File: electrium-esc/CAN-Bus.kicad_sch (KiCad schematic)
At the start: 0 parts

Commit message: Add additional connections to MCU
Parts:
- added C? (x3): 100n, symbol Device:C
- added R? (x2): 10, symbol Device:R
- added R?: IN, symbol Device:R
- added U?: SN65HVD232, Package_SO:SOIC-8_3.9x4.9mm_P1.27mm, symbol Interface_CAN_LIN:SN65HVD232
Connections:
- new net: C?.2, R?.2, U?.1 (D)
- new net: R?.1, U?.4 (R)
- new net +3.3V: C?.1, C?.1, C?.1, U?.3 (VCC)
- new net CANH: R?.1, U?.7 (CANH)
- new net CANL: R?.2, U?.6 (CANL)
- new net CAN_RX: R?.2
- new net CAN_TX: R?.1
- new net GND: C?.2, C?.2, U?.2 (GND)
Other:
- note added: "Can even be 0"
- company: (none) -> Electrium Mobility
- title: (none) -> BLDC Electronic Speed Controller 1.0

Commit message: Fix Error
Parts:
- C49, C50, C51: renamed from C?; footprint (none) -> Capacitor_SMD:C_0603_1608Metric
- R41, R42, R43: renamed from R?; footprint (none) -> Resistor_SMD:R_0603_1608Metric
- gave numbers to parts that had none: 1
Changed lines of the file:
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@@
   (symbol (lib_id "Interface_CAN_LIN:SN65HVD232") (at 144.78 92.71 0) (unit 1)
     (in_bom yes) (on_board yes) (fields_autoplaced)
-    (property "Reference" "U?" (id 0) (at 146.7994 82.55 0)
+    (property "Reference" "U3" (id 0) (at 146.7994 82.55 0)
       (effects (font (size 1.27 1.27)) (justify left))
     )
@@
   (symbol (lib_id "power:GND") (at 154.94 77.47 0) (unit 1)
     (in_bom yes) (on_board yes) (fields_autoplaced)
-    (property "Reference" "#PWR?" (id 0) (at 154.94 83.82 0)
+    (property "Reference" "#PWR0153" (id 0) (at 154.94 83.82 0)
       (effects (font (size 1.27 1.27)) hide)
     )
@@
   (symbol (lib_id "power:GND") (at 167.64 77.47 0) (unit 1)
     (in_bom yes) (on_board yes) (fields_autoplaced)
-    (property "Reference" "#PWR?" (id 0) (at 167.64 83.82 0)
+    (property "Reference" "#PWR0152" (id 0) (at 167.64 83.82 0)
       (effects (font (size 1.27 1.27)) hide)
     )
@@
   (symbol (lib_id "power:GND") (at 144.78 102.87 0) (unit 1)
     (in_bom yes) (on_board yes) (fields_autoplaced)
-    (property "Reference" "#PWR?" (id 0) (at 144.78 109.22 0)
+    (property "Reference" "#PWR0150" (id 0) (at 144.78 109.22 0)
       (effects (font (size 1.27 1.27)) hide)
     )
@@
   (symbol (lib_id "Device:C") (at 154.94 73.66 0) (unit 1)
     (in_bom yes) (on_board yes) (fields_autoplaced)
-    (property "Reference" "C?" (id 0) (at 158.75 72.3899 0)
+    (property "Reference" "C50" (id 0) (at 158.75 72.3899 0)
       (effects (font (size 1.27 1.27)) (justify left))
     )
@@
       (effects (font (size 1.27 1.27)) (justify left))
     )
-    (property "Footprint" "" (id 2) (at 155.9052 77.47 0)
+    (property "Footprint" "Capacitor_SMD:C_0603_1608Metric" (id 2) (at 155.9052 77.47 0)
       (effects (font (size 1.27 1.27)) hide)
     )
@@
   (symbol (lib_id "Device:R") (at 130.81 90.17 90) (unit 1)
     (in_bom yes) (on_board yes)
-    (property "Reference" "R?" (id 0) (at 130.81 87.63 90))
+    (property "Reference" "R41" (id 0) (at 130.81 87.63 90))
     (property "Value" "10" (id 1) (at 130.81 90.17 90))
-    (property "Footprint" "" (id 2) (at 130.81 91.948 90)
+    (property "Footprint" "Resistor_SMD:R_0603_1608Metric" (id 2) (at 130.81 91.948 90)
       (effects (font (size 1.27 1.27)) hide)
     )
@@
   (symbol (lib_id "Device:R") (at 130.81 92.71 270) (unit 1)
     (in_bom yes) (on_board yes)
-    (property "Reference" "R?" (id 0) (at 130.81 95.25 90))
+    (property "Reference" "R42" (id 0) (at 130.81 95.25 90))
     (property "Value" "10" (id 1) (at 130.81 92.71 90))
-    (property "Footprint" "" (id 2) (at 130.81 90.932 90)
+    (property "Footprint" "Resistor_SMD:R_0603_1608Metric" (id 2) (at 130.81 90.932 90)
       (effects (font (size 1.27 1.27)) hide)
     )
@@
   (symbol (lib_id "Device:C") (at 167.64 73.66 0) (unit 1)
     (in_bom yes) (on_board yes) (fields_autoplaced)
-    (property "Reference" "C?" (id 0) (at 171.45 72.3899 0)
+    (property "Reference" "C51" (id 0) (at 171.45 72.3899 0)
       (effects (font (size 1.27 1.27)) (justify left))
     )
@@
       (effects (font (size 1.27 1.27)) (justify left))
     )
-    (property "Footprint" "" (id 2) (at 168.6052 77.47 0)
+    (property "Footprint" "Capacitor_SMD:C_0603_1608Metric" (id 2) (at 168.6052 77.47 0)
       (effects (font (size 1.27 1.27)) hide)
     )
@@
   (symbol (lib_id "Device:C") (at 134.62 74.93 0) (unit 1)
     (in_bom yes) (on_board yes) (fields_autoplaced)
-    (property "Reference" "C?" (id 0) (at 138.43 73.6599 0)
+    (property "Reference" "C49" (id 0) (at 138.43 73.6599 0)
       (effects (font (size 1.27 1.27)) (justify left))
     )
@@
       (effects (font (size 1.27 1.27)) (justify left))
     )
-    (property "Footprint" "" (id 2) (at 135.5852 78.74 0)
+    (property "Footprint" "Capacitor_SMD:C_0603_1608Metric" (id 2) (at 135.5852 78.74 0)
       (effects (font (size 1.27 1.27)) hide)
     )
@@
   (symbol (lib_id "Device:R") (at 165.1 93.98 0) (unit 1)
     (in_bom yes) (on_board yes) (fields_autoplaced)
-    (property "Reference" "R?" (id 0) (at 167.64 92.7099 0)
+    (property "Reference" "R43" (id 0) (at 167.64 92.7099 0)
       (effects (font (size 1.27 1.27)) (justify left))
     )
@@
       (effects (font (size 1.27 1.27)) (justify left))
     )
-    (property "Footprint" "" (id 2) (at 163.322 93.98 90)
+    (property "Footprint" "Resistor_SMD:R_0603_1608Metric" (id 2) (at 163.322 93.98 90)
       (effects (font (size 1.27 1.27)) hide)
     )
@@
   (symbol (lib_id "power:+3.3V") (at 144.78 69.85 0) (unit 1)
     (in_bom yes) (on_board yes) (fields_autoplaced)
-    (property "Reference" "#PWR?" (id 0) (at 144.78 73.66 0)
+    (property "Reference" "#PWR0151" (id 0) (at 144.78 73.66 0)
       (effects (font (size 1.27 1.27)) hide)
     )

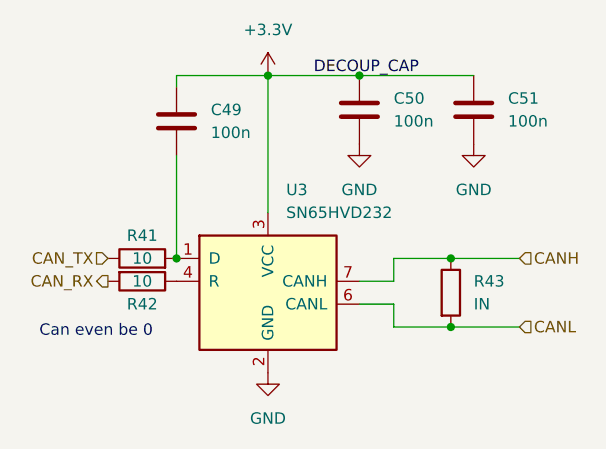
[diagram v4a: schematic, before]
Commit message: relabel components to make more sense
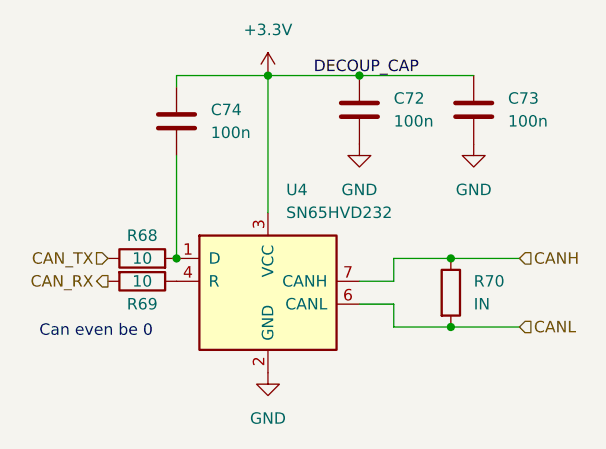
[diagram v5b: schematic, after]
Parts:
- renumbered C50 to C72, C51 to C73, C49 to C74, R41 to R68, R42 to R69, R43 to R70, U3 to U4
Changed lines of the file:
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@@
   (symbol (lib_id "Interface_CAN_LIN:SN65HVD232") (at 144.78 92.71 0) (unit 1)
     (in_bom yes) (on_board yes) (fields_autoplaced)
-    (property "Reference" "U3" (id 0) (at 146.7994 82.55 0)
+    (property "Reference" "U4" (id 0) (at 146.7994 82.55 0)
       (effects (font (size 1.27 1.27)) (justify left))
     )
@@
   (symbol (lib_id "power:GND") (at 154.94 77.47 0) (unit 1)
     (in_bom yes) (on_board yes) (fields_autoplaced)
-    (property "Reference" "#PWR0153" (id 0) (at 154.94 83.82 0)
+    (property "Reference" "#PWR068" (id 0) (at 154.94 83.82 0)
       (effects (font (size 1.27 1.27)) hide)
     )
@@
   (symbol (lib_id "power:GND") (at 167.64 77.47 0) (unit 1)
     (in_bom yes) (on_board yes) (fields_autoplaced)
-    (property "Reference" "#PWR0152" (id 0) (at 167.64 83.82 0)
+    (property "Reference" "#PWR069" (id 0) (at 167.64 83.82 0)
       (effects (font (size 1.27 1.27)) hide)
     )
@@
   (symbol (lib_id "power:GND") (at 144.78 102.87 0) (unit 1)
     (in_bom yes) (on_board yes) (fields_autoplaced)
-    (property "Reference" "#PWR0150" (id 0) (at 144.78 109.22 0)
+    (property "Reference" "#PWR070" (id 0) (at 144.78 109.22 0)
       (effects (font (size 1.27 1.27)) hide)
     )
@@
   (symbol (lib_id "Device:C") (at 154.94 73.66 0) (unit 1)
     (in_bom yes) (on_board yes) (fields_autoplaced)
-    (property "Reference" "C50" (id 0) (at 158.75 72.3899 0)
+    (property "Reference" "C72" (id 0) (at 158.75 72.3899 0)
       (effects (font (size 1.27 1.27)) (justify left))
     )
@@
   (symbol (lib_id "Device:R") (at 130.81 90.17 90) (unit 1)
     (in_bom yes) (on_board yes)
-    (property "Reference" "R41" (id 0) (at 130.81 87.63 90))
+    (property "Reference" "R68" (id 0) (at 130.81 87.63 90))
     (property "Value" "10" (id 1) (at 130.81 90.17 90))
     (property "Footprint" "Resistor_SMD:R_0603_1608Metric" (id 2) (at 130.81 91.948 90)
@@
   (symbol (lib_id "Device:R") (at 130.81 92.71 270) (unit 1)
     (in_bom yes) (on_board yes)
-    (property "Reference" "R42" (id 0) (at 130.81 95.25 90))
+    (property "Reference" "R69" (id 0) (at 130.81 95.25 90))
     (property "Value" "10" (id 1) (at 130.81 92.71 90))
     (property "Footprint" "Resistor_SMD:R_0603_1608Metric" (id 2) (at 130.81 90.932 90)
@@
   (symbol (lib_id "Device:C") (at 167.64 73.66 0) (unit 1)
     (in_bom yes) (on_board yes) (fields_autoplaced)
-    (property "Reference" "C51" (id 0) (at 171.45 72.3899 0)
+    (property "Reference" "C73" (id 0) (at 171.45 72.3899 0)
       (effects (font (size 1.27 1.27)) (justify left))
     )
@@
   (symbol (lib_id "Device:C") (at 134.62 74.93 0) (unit 1)
     (in_bom yes) (on_board yes) (fields_autoplaced)
-    (property "Reference" "C49" (id 0) (at 138.43 73.6599 0)
+    (property "Reference" "C74" (id 0) (at 138.43 73.6599 0)
       (effects (font (size 1.27 1.27)) (justify left))
     )
@@
   (symbol (lib_id "Device:R") (at 165.1 93.98 0) (unit 1)
     (in_bom yes) (on_board yes) (fields_autoplaced)
-    (property "Reference" "R43" (id 0) (at 167.64 92.7099 0)
+    (property "Reference" "R70" (id 0) (at 167.64 92.7099 0)
       (effects (font (size 1.27 1.27)) (justify left))
     )
@@
   (symbol (lib_id "power:+3.3V") (at 144.78 69.85 0) (unit 1)
     (in_bom yes) (on_board yes) (fields_autoplaced)
-    (property "Reference" "#PWR0151" (id 0) (at 144.78 73.66 0)
+    (property "Reference" "#PWR067" (id 0) (at 144.78 73.66 0)
       (effects (font (size 1.27 1.27)) hide)
     )
